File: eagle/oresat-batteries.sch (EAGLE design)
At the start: 318 parts, among them J1 J-SAMTEC-TFM-120-X1-XXX-D-RA, J4 ORESAT-DEBUG-CONNECTOR-ALL, Q1 DMP2240UDM, Q10 NTR4101, Q11 PMV45EN, Q12 Si7625DN, Q13 Si7625DN, Q14 NTR4101, Q15 NTR4101, Q16 Si7625DN, Q17 Si7625DN, Q18 Si7625DN, Q19 Si7625DN, Q2 PMV45EN, Q20 Si7625DN, Q21 PMV45EN, Q22 PMV45EN, Q23 NTR4101, Q24 PM45VEN, Q25 PM45VEN, Q26 PM45VEN, Q27 PM45VEN, Q28 NTR4101, Q29 PM45VEN, Q3 DMP3050LVT-7, Q30 Si7625DN, Q31 Si7625DN, Q32 NTR4101, Q33 NTR4101, Q34 Si7625DN, Q35 Si7625DN, Q36 Si7625DN, Q37 Si7625DN, Q38 Si7625DN, Q39 PM45VEN, Q4 DMP3050LVT-7, Q40 PM45VEN, Q41 NTR4101, Q42 DMP2240UDM, Q43 DMP2240UDM, Q44 PMV45EN, Q45 FDMQ86530L_2-GATES, Q5 PMV45EN, Q6 PM45VEN, Q7 PM45VEN, Q8 PM45VEN, Q9 PM45VEN, U1 MAX7310ATE, U10 LTC4412, U11 LTC4412, U12 MAX17205G, U13 S-8209AAA-T8T1U, U14 S-8209AAA-T8T1U, U15 LTC4412, U16 LTC4412, U17 MAX17205G, U2 MIC842LYC5, U20 TCAN330, U21 STM32F091C, U3 MIC842LYC5, U4 MAX4211FETE, U5 TPS62111RSA, U8 S-8209AAA-T8T1U, U9 S-8209AAA-T8T1U, X3 16MHZ-2.5x2mm

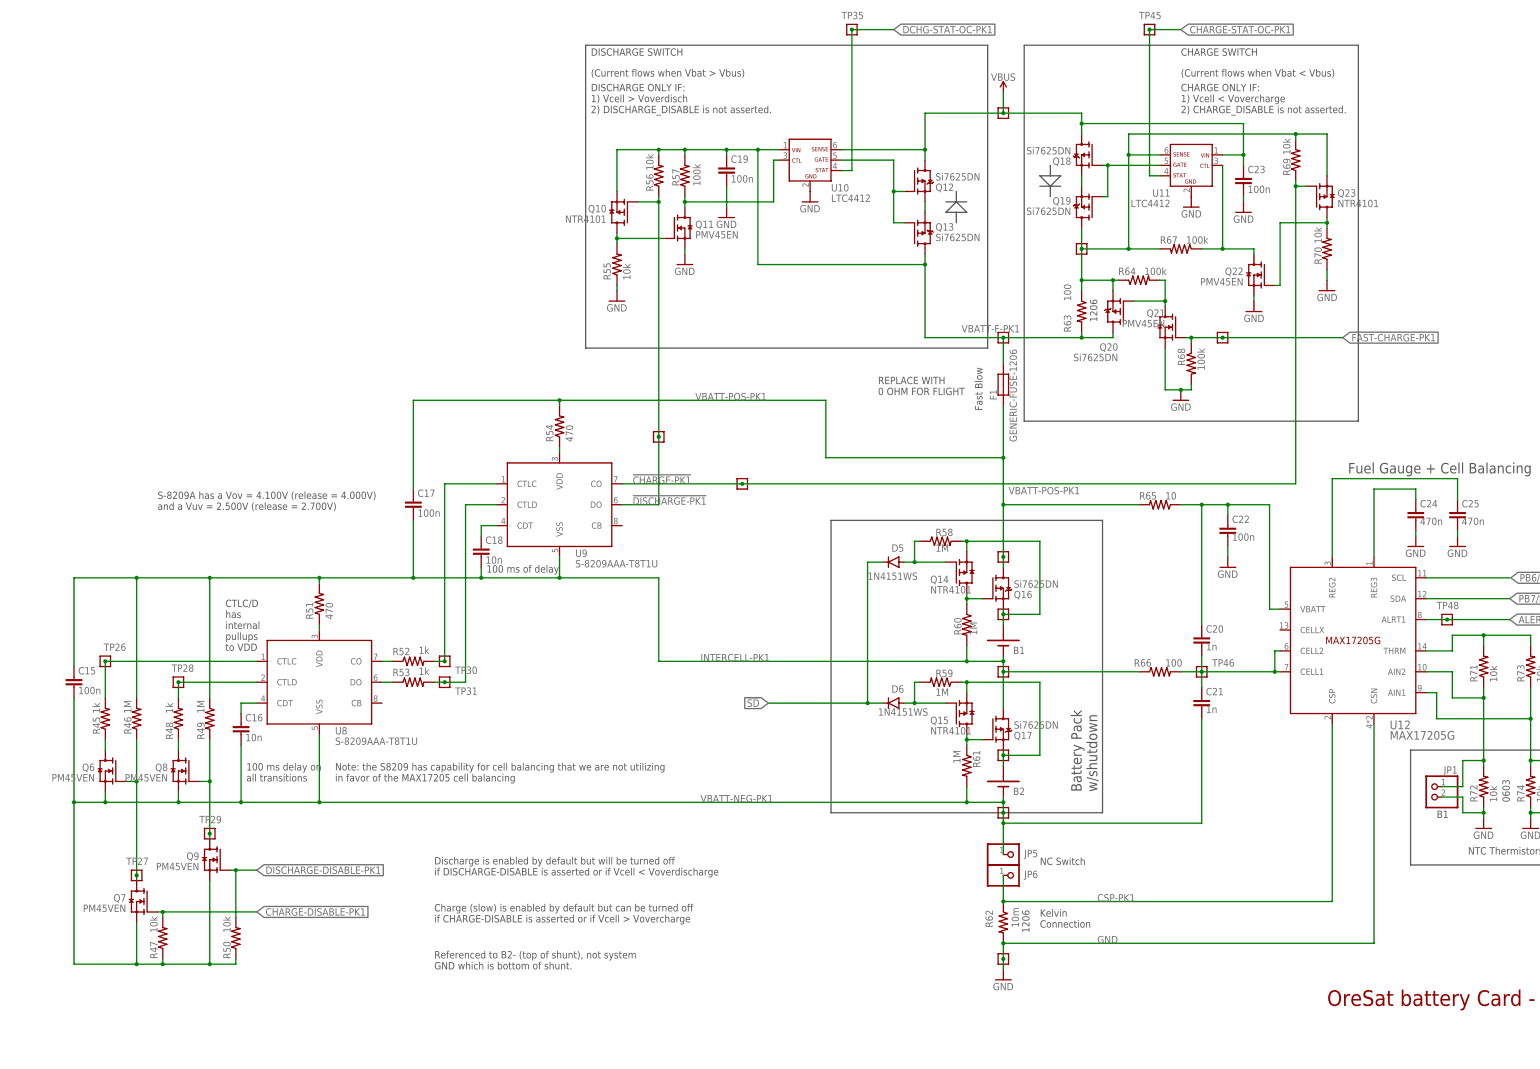
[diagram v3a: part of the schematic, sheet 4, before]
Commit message: OreSat Battery Card v2.0
Changes based on finally fixing the C3 watchdog timer and the interactions between the two.

- Moved right hand ground cut switch to vbat switch. This solves a *lot* of problems with removing the ground and shutdown not working correctly.
- Got rid of "fast charge" and split the charge / discharge paths with independent PTC (5A out, 2A in).
- Switched most everytthing to 100k. 1M wasn't enough to overcome leakage, and 10k was too much.
- Fixed the ablic bypass cap which should have gone right to VDD.
- Rerouted !SD for lots of paranoia.
- Rev'd board to v2.0
- Changed to latest OreSat card outline (v1.3).
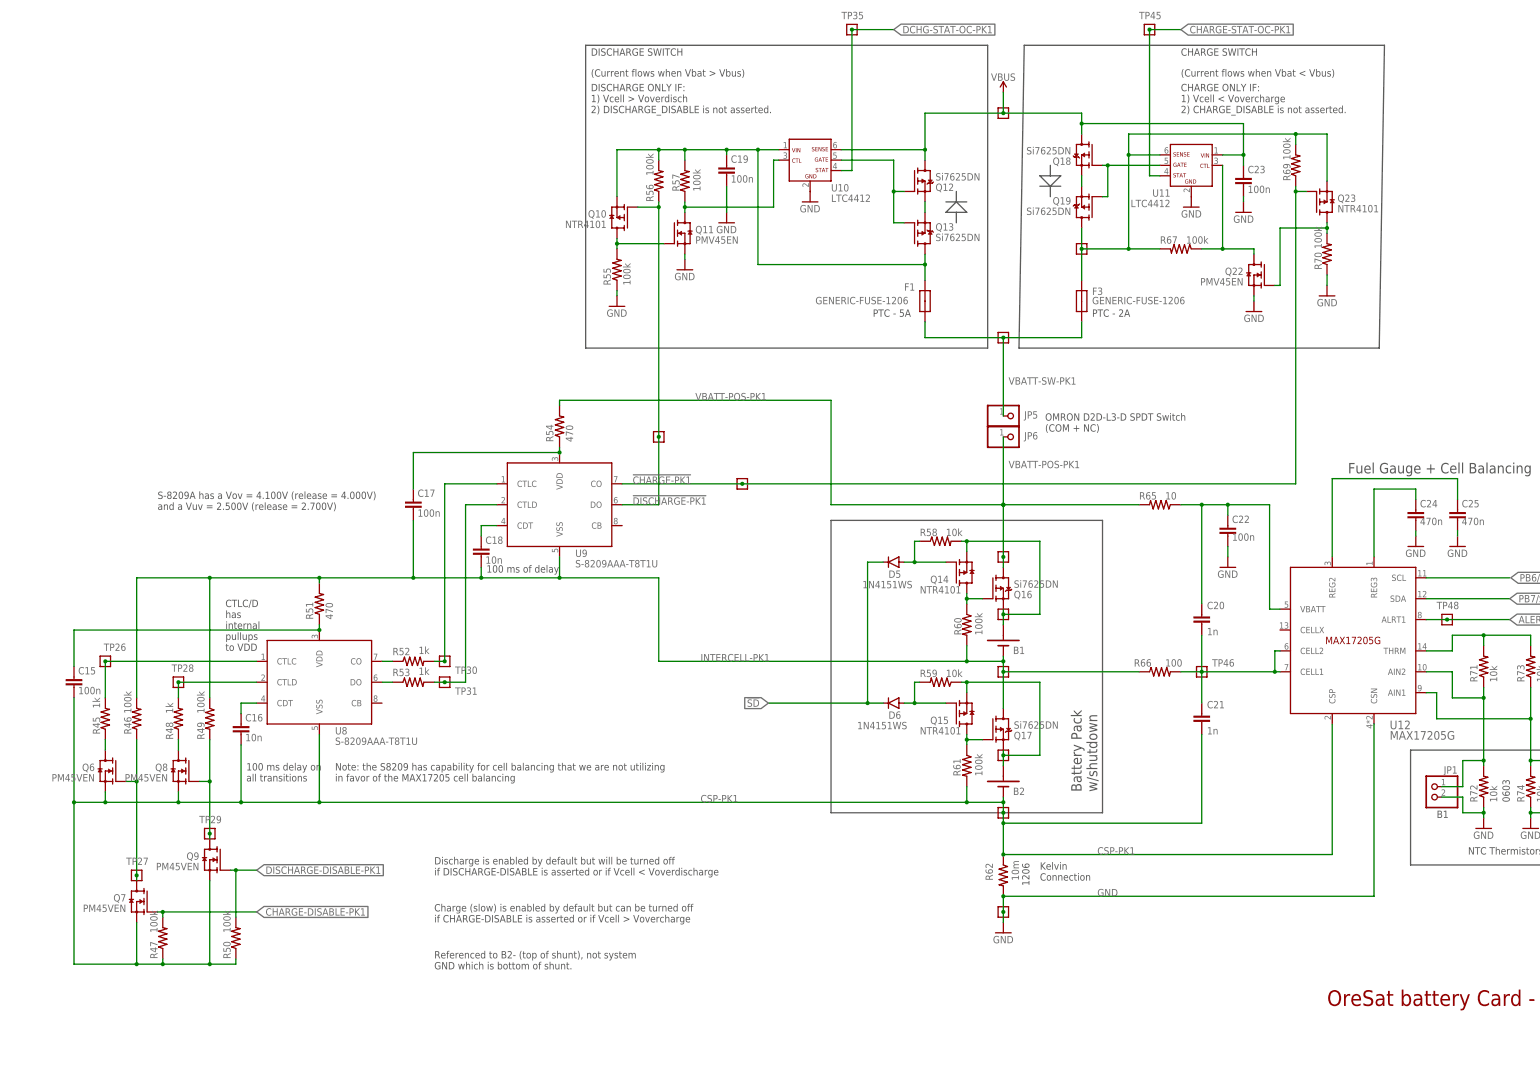
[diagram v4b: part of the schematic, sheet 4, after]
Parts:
- removed PCB2: ORESAT-CARD-V1.1-BATTERY-V1.0, oresat-cards:ORESAT-CARD-V1.1-BATTERY-V1.0
- removed Q20, Q38: Si7625DN, Q-VIshay-MOSFET-PCH-PowerPak121-8:Q-VISHAY-MOSFET-PCH-POWERPAK-1212-8
- removed Q21: PMV45EN, Q-MOSFET-NCH-SOT23-3:N-MOSFET-SOT-23-3
- removed Q39: PM45VEN, Q-MOSFET-NCH-SOT23-3:N-MOSFET-SOT-23-3
- removed R63, R93: 100, oresat-rcl:R-US_1206-C
- removed R64, R68, R94, R98: 100k, oresat-rcl:R-US_0603-C-NOSILK
- removed TP47, TP70: TEST-POINT-LARGE-SQUARE, oresat-misc:TEST-POINT-LARGE-SQUARE
- added F3, F4: GENERIC-FUSE-1206, F-Generic-Fuse-1206:GENERIC-FUSE-1206
- added PCB1: ORESAT-CARD-V1.3-BATTERY, oresat-cards:ORESAT-CARD-V1.3-BATTERY
- R100, R47, R50, R55, R56, R69, R70, R77, R80, R85, R86, R99: value 10k -> 100k
- R46, R49, R60, R61, R76, R79: value 1M -> 100k
- R58, R59: value 1M -> 10k
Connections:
- removed net !FAST-CHARGE-PK1: Q20.G, Q21.D, R64.2
- removed net !FAST-CHARGE-PK2: Q38.G, Q39.D, R94.2
- removed net FAST-CHARGE-PK1: Q21.G, R68.1, TP47.1, U21.PA6
- removed net FAST-CHARGE-PK2: Q39.G, R98.1, TP70.1, U21.PB2
- removed net VBATT-NEG-PK1: B2.NEG, C15.2, C16.2, C21.2, JP5.1, Q6.S, Q7.S, Q8.S, Q9.S, R47.1, R50.1, R61.2, TP42.1, U8.VSS
- removed net VBATT-NEG-PK2: B4.NEG, C26.2, C27.2, C32.2, JP7.1, Q24.S, Q25.S, Q26.S, Q27.S, R77.1, R80.1, R91.2, TP65.1, U13.VSS
- new net VBATT-SW-PK1: F1.P$2, F3.P$2, JP5.1, TP37.1
- new net VBATT-SW-PK2: F2.P$2, F4.P$2, JP7.1, TP60.1
- net CSP-PK1: now also B2.NEG, C15.2, C16.2, C21.2, Q6.S, Q7.S, Q8.S, Q9.S, R47.1, R50.1, R61.2, TP42.1, U8.VSS; no longer JP6.1
- net CSP-PK2: now also B4.NEG, C26.2, C27.2, C32.2, Q24.S, Q25.S, Q26.S, Q27.S, R77.1, R80.1, R91.2, TP65.1, U13.VSS; no longer JP12.1
- net GND: no longer Q21.S, Q39.S, R68.2, R98.2
- net INTERCELL-PK1: no longer C15.1
- net INTERCELL-PK2: no longer C26.1
- net N$16: now also C17.1
- net N$17: now also C15.1
- net N$41: now also F3.P$1; no longer Q20.S, R63.1, R64.1
- net N$70: now also C28.1
- net N$71: now also C26.1
- net N$89: now also F4.P$1; no longer Q38.S, R93.1, R94.1
- net VBATT-F-PK1: no longer Q20.D, R63.2, TP37.1
- net VBATT-F-PK2: no longer Q38.D, R93.2, TP60.1
- net VBATT-POS-PK1: now also JP6.1; no longer C17.1, F1.P$2
- net VBATT-POS-PK2: now also JP12.1; no longer C28.1, F2.P$2
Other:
- note added: "2x OMRON D2D-L3-D SPDT Switch (COM + NO connected)"
- note added: "OMROM D2D-L3-D SPDT Swith (COM + NC)"
- note added: "OMRON D2D-L3-D SPDT Switch (COM + NC)"
- note added: "PTC - 2A"
- note added: "PTC - 5A"
- note added: "PTC-2A"
- note added: "PTC-5A"
- note removed: "Fast Blow"
- note removed: "NC Switch"
- note removed: "REPLACE WITH 0 OHM FOR FLIGHT"
- moved on the sheet: C20, C21, C31, C32, F1, F2, JP12, JP5, JP6, JP7, Q10, Q11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
